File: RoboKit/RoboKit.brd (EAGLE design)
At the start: 160 x 100 mm, 27 parts, among them CON1 XT30UPB-M, CON2 XT30UPB-M, P1 B6B-PH-K, P2 B6B-PH-K, U1 SSM6J808R, X1 JST-XH-06-PIN-LONG-PAD, X2 JST-XH-06-PIN-LONG-PAD, X3 JST-XH-02-PIN-LONG-PAD, X4 JST-XH-02-PIN-LONG-PAD, X5 JST-XH-04-PIN-LONG-PAD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

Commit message: make_circuit
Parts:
- removed X1, X2: JST-XH-06-PIN-LONG-PAD, JST XH Connectors:JST-XH-06-PACKAGE-LONG-PAD
- added CONNECTOR1: RESISTER, resistor:RESISTER_SOCKET
- added S1: (no value), switch-omron:B3F-10XX
- added TC4052DP: (no value), ic-package:DIL16
- added X7: JST-XH-10-PIN-LONG-PAD, Rembrandt Electronics - JST XH Connectors v1-0:JST-XH-10-PACKAGE-LONG-PAD
- added X8: JST-XH-02-PIN-LONG-PAD, Rembrandt Electronics - JST XH Connectors v1-0:JST-XH-02-PACKAGE-LONG-PAD
- added X9: JST-XH-03-PIN-LONG-PAD, Rembrandt Electronics - JST XH Connectors v1-0:JST-XH-03-PACKAGE-LONG-PAD
- moved X5 143.9 mm to (66.4, 69.2)
- moved X6 143.3 mm to (66.4, 60.3)
- moved X4 105.9 mm to (21.6, 66.4)
- moved X3 91.8 mm to (8.57, 66.7)
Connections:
- removed net +5V: X1.2, X2.2
- removed net ADC0: U$1.31
- removed net ADC1: U$1.32
- removed net IO16: U$1.21
- removed net IO17: U$1.22
- removed net LINE: X1.3, X2.3
- removed net MD_INA_L: U$2.INA1, U$2.INA2
- removed net MD_INA_R: U$3.INA1, U$3.INA2
- removed net MD_INB_L: U$2.INB1, U$2.INB2
- removed net MD_INB_R: U$3.INB1, U$3.INB2
- removed net MOTER_A_L: X3.1
- removed net MOTER_A_R: X4.1
- removed net MOTER_B_L: X3.2
- removed net MOTER_B_R: X4.2
- removed net MUX0: X1.4, X2.4
- removed net MUX1: X1.5, X2.5
- removed net MUX2: X1.6, X2.6
- new net 0X: TC4052DP.12, X7.3
- new net 0Y: TC4052DP.1, X7.7
- new net 1X: TC4052DP.14, X7.4
- new net 1Y: TC4052DP.5, X7.8
- new net 2X: TC4052DP.15, X7.5
- new net 2Y: TC4052DP.2, X7.9
- new net 3X: TC4052DP.11, X7.6
- new net 3Y: TC4052DP.4, X7.10
- new net A: TC4052DP.10, U$1.21
- new net B: TC4052DP.9, U$1.22
- new net N$4: CONNECTOR1.2, S1.3
- new net X-COM: TC4052DP.13, U$1.32
- new net Y-COM: TC4052DP.3, U$1.31
- net 3V3: now also CONNECTOR1.1
- net GND: now also S1.2, TC4052DP.6, TC4052DP.7, TC4052DP.8, X7.1, X8.2, X9.2; no longer X1.1, X2.1
- net IO0: now also U$2.INA1, U$2.INB1
- net IO1: now also U$2.INA2, U$2.INB2
- net IO2: now also U$3.INA1, U$3.INB1
- net IO21: now also S1.4
- net IO3: now also U$3.INA2, U$3.INB2
- net IO7: now also X8.1
- net MOTOR_A_L: now also X3.1
- net MOTOR_A_R: now also X4.1
- net MOTOR_B_L: now also X3.2
- net MOTOR_B_R: now also X4.2
- net VBUS: now also TC4052DP.16, X7.2, X9.1
- net VOUT: now also X9.3
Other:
- board size 160 x 100 mm -> 134 x 82 mm

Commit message: make_okunishi_1
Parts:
- moved X4 80.3 mm to (98.7, 44.1), turned to 90 degrees
- moved U$3 72.0 mm to (88.3, 62.9)
- moved X9 54.3 mm to (31.1, 28.6)
- moved X6 50.8 mm to (100.3, 22.5), turned to 270 degrees
- moved X8 41.0 mm to (86.4, 44.5)
- moved U$4 40.5 mm to (34.9, 17.8)
- moved X3 35.2 mm to (35.6, 44.1), turned to 270 degrees
- moved U$2 30.7 mm to (46.4, 62.9)
- moved P1 30.1 mm to (98.7, 63.2), turned to 90 degrees
- moved U$1 29.2 mm to (66.4, 45.1)
- moved TC4052DP 27.6 mm to (47.0, 39.1), turned to 90 degrees
- moved X7 21.0 mm to (91.8, 22.2), turned to 270 degrees
- moved P2 18.6 mm to (35.6, 63.2), turned to 270 degrees
- moved S1 17.6 mm to (95.2, 76.5)
- moved CONNECTOR1 10.8 mm to (81.0, 74.3)
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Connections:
- net 3V3_EN: now also X6.1
- net VCC: no longer X6.1
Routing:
- net GND: track 0.00 -> 329.6 mm, vias 0 -> 3
- net SDA: track 0.00 -> 168.8 mm
- net VBUS: track 0.00 -> 159.1 mm, vias 0 -> 2
- net SCL: track 0.00 -> 155.0 mm
- net VCC: track 0.00 -> 139.1 mm
- net VOUT: track 30.6 -> 142.7 mm
- net 3Y: track 0.00 -> 89.4 mm
- net 3X: track 0.00 -> 83.4 mm
- net IO0: track 0.00 -> 76.8 mm
- net 0X: track 0.00 -> 74.8 mm, vias 0 -> 1
- net 2X: track 0.00 -> 74.6 mm
- net 1Y: track 0.00 -> 57.3 mm
- net IO21: track 0.00 -> 56.1 mm
- net 1X: track 0.00 -> 55.9 mm
- net 2Y: track 0.00 -> 54.3 mm
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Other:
- outline, holes or cut-outs redrawn

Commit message: 回路図の完成
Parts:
- added S2: (no value), switch:320-916
- moved CON2 77.6 mm to (38.1, 76.8)
- moved X6 63.7 mm to (66.0, 76.2), turned to 0 degrees
- moved X5 62.3 mm to (99.4, 22.9), turned to 270 degrees
- moved TC4052DP 42.0 mm to (87.3, 27.3)
- moved X7 28.3 mm to (67.0, 8.57), turned to 0 degrees
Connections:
- removed net IO10: U$1.14
- removed net IO11: U$1.15
- removed net IO12: U$1.16
- removed net IO13: U$1.17
- removed net IO4: U$1.6
- removed net IO5: U$1.7
- new net 5.0V: S2.2, X9.1
- net HALL_A_L: now also U$1.16
- net HALL_A_R: now also U$1.14
- net HALL_B_L: now also U$1.17
- net HALL_B_R: now also U$1.15
- net SCL: now also U$1.7
- net SDA: now also U$1.6
- net VBUS: now also S2.3; no longer X9.1
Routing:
- net GND: track 329.6 -> 2.79 mm, vias 3 -> 0
- net SDA: track 168.8 -> 1.30 mm
- net VBUS: track 159.1 -> 0.00 mm, vias 2 -> 0
- net SCL: track 155.0 -> 0.00 mm
- net VCC: track 139.1 -> 0.00 mm
- net VOUT: track 142.7 -> 30.7 mm
- net 3Y: track 89.4 -> 0.00 mm
- net 3X: track 83.4 -> 0.10 mm
- net IO0: track 76.8 -> 0.00 mm
- net 0X: track 74.8 -> 0.00 mm, vias 1 -> 0
- net 2X: track 74.6 -> 0.00 mm
- net 1Y: track 57.3 -> 0.00 mm
- net 1X: track 55.9 -> 0.00 mm
- net IO21: track 56.1 -> 0.89 mm
- net 2Y: track 54.3 -> 0.00 mm
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
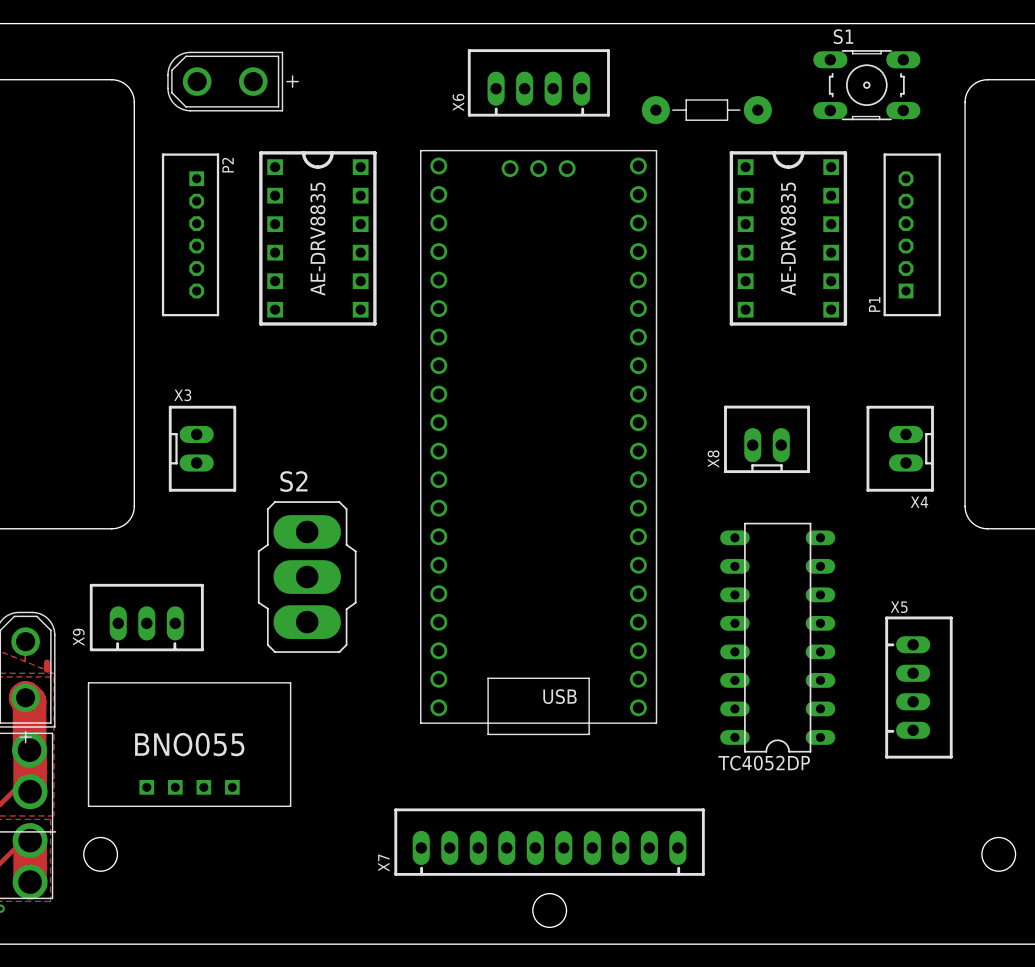
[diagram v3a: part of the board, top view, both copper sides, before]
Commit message: ボードのグランド以外を配置
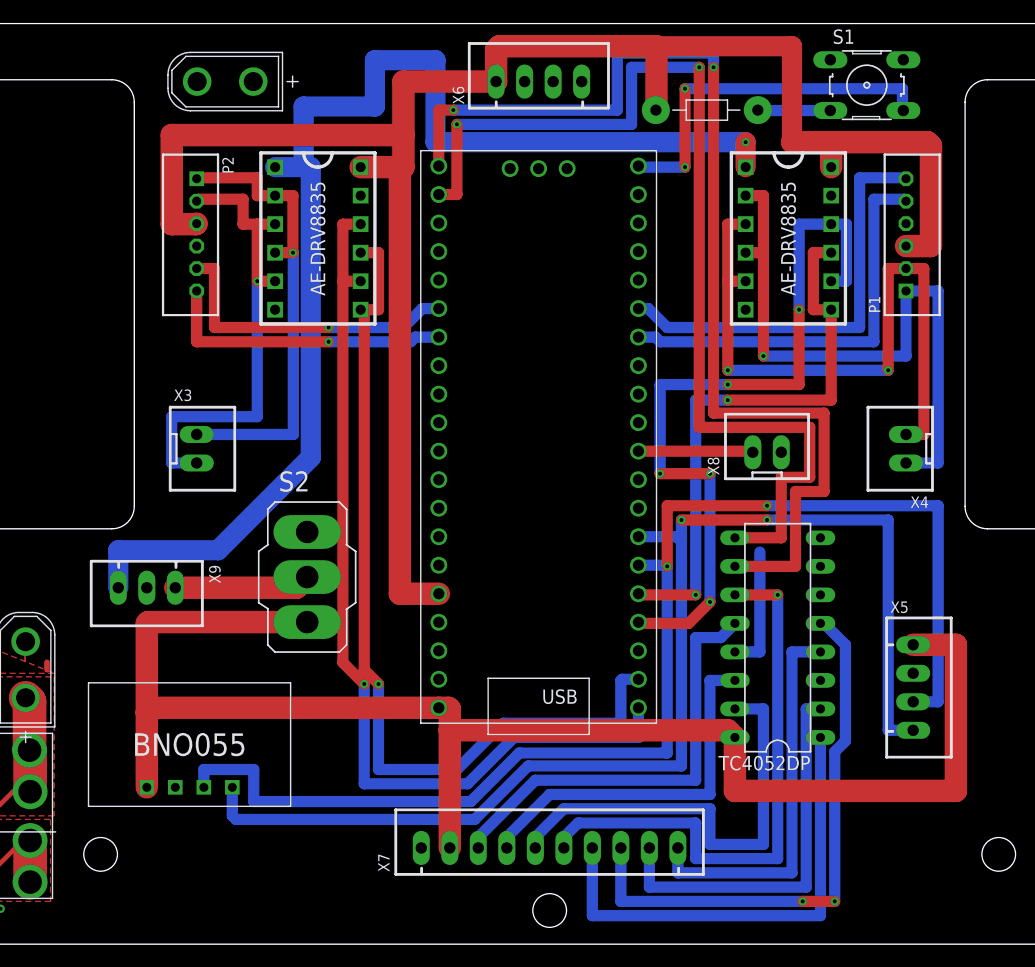
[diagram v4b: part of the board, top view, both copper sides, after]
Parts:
- moved X9 3.18 mm to (31.1, 31.8), turned to 180 degrees
- moved X8 0.64 mm to (86.4, 43.8)
- moved X6 0.63 mm to (66.0, 76.8)
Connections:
- removed net IO20: U$1.26
- removed net VCC: P1.3, P2.3, U$2.VCC, U$3.VCC, U$4.VIN
- new net IO12: U$1.16
- new net IO13: U$1.17
- net 3V3: now also P1.3, P2.3, U$2.VCC, U$3.VCC, X6.1
- net 3V3_EN: no longer X6.1
- net HALL_A_L: now also U$1.26; no longer U$1.16
- net HALL_B_L: now also U$1.27; no longer U$1.17
- net IO0: now also U$2.INA2; no longer U$2.INB1
- net IO1: now also U$2.INB1; no longer U$2.INA2
- net IO15: now also S1.4
- net IO2: now also U$3.INA2; no longer U$3.INB1
- net IO21: no longer S1.4, U$1.27
- net IO3: now also U$3.INB1; no longer U$3.INA2
- net MOTOR_A_L: now also U$2.AOUT2; no longer U$2.BOUT1
- net MOTOR_A_R: now also U$3.AOUT2; no longer U$3.BOUT1
- net MOTOR_B_L: now also U$2.BOUT1; no longer U$2.AOUT2
- net MOTOR_B_R: now also U$3.BOUT1; no longer U$3.AOUT2
- net VBUS: now also U$4.VIN
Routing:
- net 3V3: track 0.03 -> 161.4 mm
- net VBUS: track 0.00 -> 135.5 mm
- net SDA: track 1.30 -> 116.0 mm, vias 0 -> 2
- net VOUT: track 30.7 -> 142.1 mm, vias 0 -> 1
- net SCL: track 0.00 -> 109.9 mm, vias 0 -> 2
- net A: track 0.00 -> 98.0 mm, vias 0 -> 2
- net B: track 0.00 -> 93.0 mm, vias 0 -> 2
- net IO0: track 0.00 -> 82.6 mm, vias 0 -> 1
- net IO1: track 0.03 -> 78.6 mm, vias 0 -> 1
- net IO2: track 0.00 -> 68.3 mm, vias 0 -> 5
- net MOTOR_B_R: track 0.06 -> 59.1 mm, vias 0 -> 2
- net MOTOR_A_R: track 0.05 -> 57.0 mm, vias 0 -> 1
- net 3X: track 0.10 -> 51.0 mm, vias 0 -> 1
- net IO3: track 0.00 -> 50.9 mm, vias 0 -> 2
- net 1Y: track 0.00 -> 50.1 mm, vias 0 -> 2
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
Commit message: 線を斜めに配置
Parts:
- moved CON1 5.41 mm to (20.6, 29.8)
- moved U$7 5.08 mm to (20.3, 16.5)
- moved CON2 1.59 mm to (36.5, 76.8)
- moved X3 1.59 mm to (37.1, 44.1)
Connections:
- net VBUS: no longer S2.3, TC4052DP.16, U$4.VIN, X5.1, X7.2
- net VSYS: now also S2.3, TC4052DP.16, U$4.VIN, X5.1, X7.2
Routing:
- net X-COM: track 11.1 -> 153.6 mm, vias 0 -> 4
- net VSYS: track 0.00 -> 136.6 mm
- net VBUS: track 135.5 -> 0.00 mm
- net Y-COM: track 0.00 -> 117.3 mm, vias 0 -> 6
- net VIN: track 5.01 -> 97.6 mm, vias 0 -> 1
- net SDA: track 116.0 -> 161.1 mm, vias 2 -> 3
- net SCL: track 109.9 -> 152.6 mm, vias 2 -> 3
- net VOUT: track 142.1 -> 159.7 mm, vias 1 -> 2
- net 3V3: track 161.4 -> 154.4 mm
- net MOTOR_A_L: track 41.7 -> 36.0 mm
- net GND: track 2.52 -> 8.05 mm
- net V_HIGH: track 8.74 -> 13.4 mm
- net MOTOR_B_L: track 42.0 -> 37.3 mm
- net B: track 93.0 -> 89.8 mm
- net 3Y: track 34.6 -> 31.5 mm
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
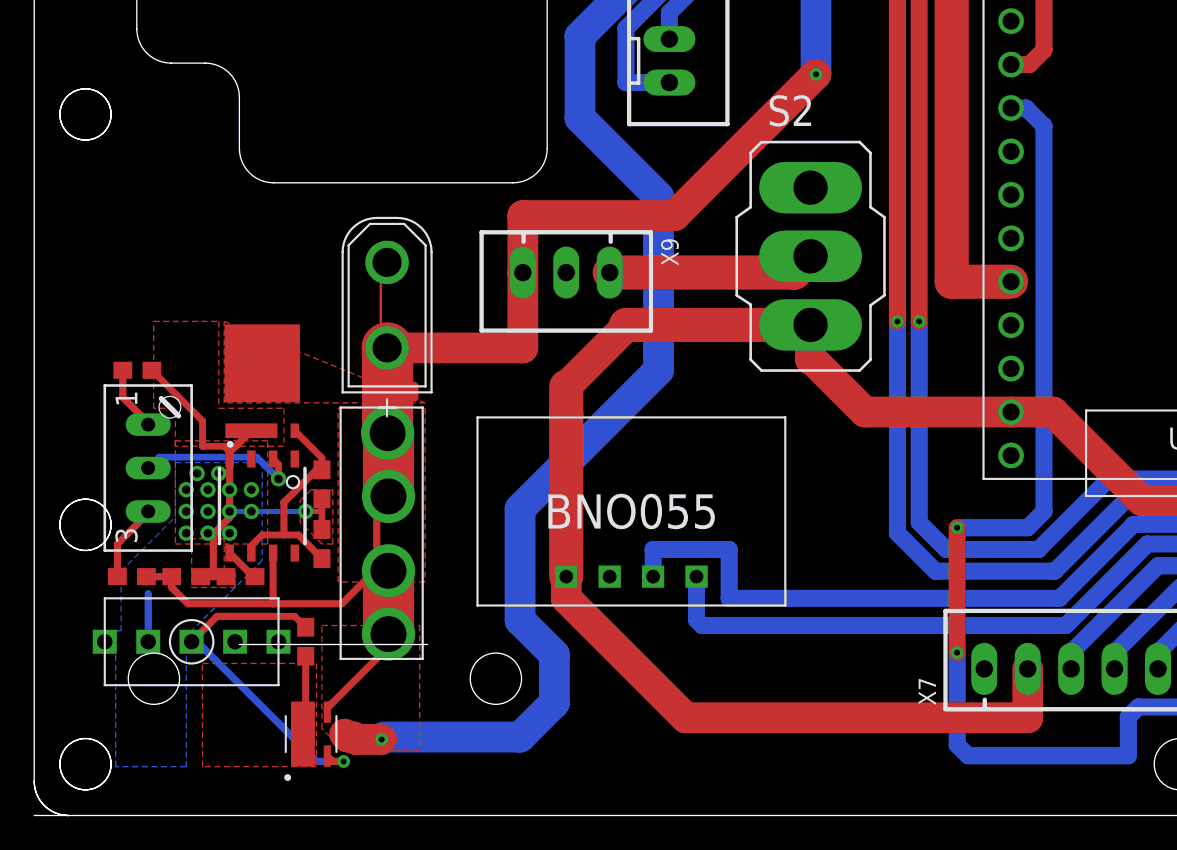
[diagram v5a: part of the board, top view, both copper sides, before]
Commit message: 保護回路の配線を設定
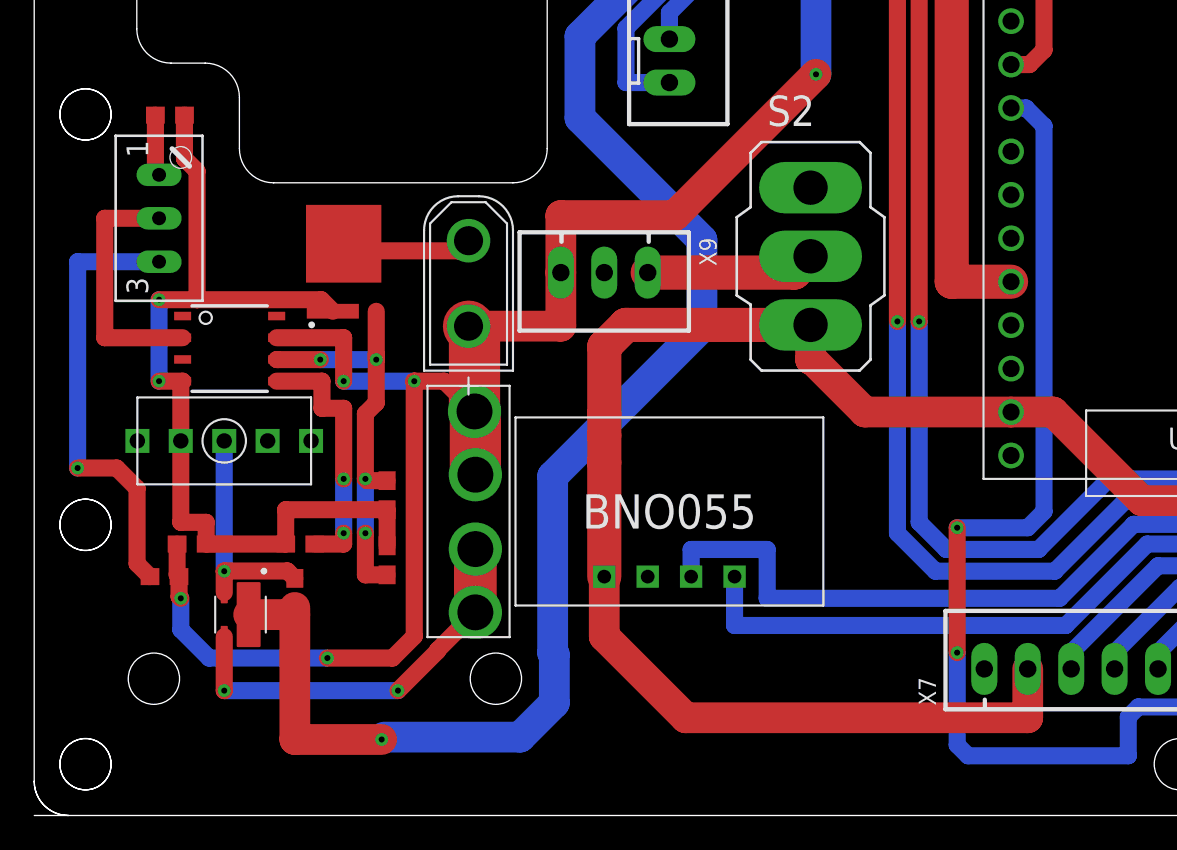
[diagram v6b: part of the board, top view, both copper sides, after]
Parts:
- moved R3 15.0 mm to (7.94, 41.0)
- moved R5 14.6 mm to (8.57, 34.9)
- moved U$9 11.9 mm to (11.1, 21.9)
- moved U$5 9.40 mm to (11.4, 27.3), turned to 0 degrees
- moved U$6 8.45 mm to (18.1, 32.4)
- moved U1 8.11 mm to (12.1, 11.7), turned to 270 degrees
- moved U$7 5.24 mm to (25.4, 17.8)
- moved CON1 4.93 mm to (25.4, 31.1)
- moved C11 3.98 mm to (15.6, 15.9)
- moved C7 3.93 mm to (20.6, 14.9)
- moved R2 3.86 mm to (20.6, 18.7)
- moved R4 2.93 mm to (15.2, 13.0)
- moved U$4 2.22 mm to (37.1, 17.8)
- moved X9 2.22 mm to (33.3, 31.8)
- moved C2 1.93 mm to (9.21, 15.9)
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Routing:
- net GND_IN: track 31.0 -> 53.4 mm, vias 14 -> 2
- net N$3: track 4.56 -> 26.3 mm, vias 0 -> 1
- net VOUT: track 159.7 -> 176.3 mm, vias 2 -> 6
- net N$5: track 2.06 -> 15.1 mm, vias 0 -> 2
- net N$6: track 13.2 -> 24.4 mm, vias 0 -> 4
- net V_HIGH: track 13.4 -> 23.5 mm, vias 0 -> 2
- net VIN: track 97.6 -> 106.1 mm
- net N$7: track 20.4 -> 13.2 mm
- net N$1: track 9.70 -> 14.7 mm, vias 1 -> 0
- net 5.0V: track 12.1 -> 9.92 mm
- net SDA: track 161.1 -> 158.9 mm
- net SCL: track 152.6 -> 150.6 mm
- net VSYS: track 136.6 -> 134.6 mm
- removed copper zone on layer 1, net GND
- removed copper zone on layer 1, net GND_IN
- removed copper zone on layer 16, net GND_IN
- removed copper zone on layer 1, net VIN
- removed copper zone on layer 1, net VOUT
- removed copper zone on layer 1, net V_HIGH
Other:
- outline, holes or cut-outs redrawn

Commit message: 一応完成
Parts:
- moved S1 2.71 mm to (92.7, 75.6)
- moved R3 0.95 mm to (6.99, 41.0)
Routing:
- net GND: track 8.26 -> 163.1 mm, vias 0 -> 6
- net 3V3: track 154.4 -> 168.9 mm
- net VSYS: track 134.6 -> 137.8 mm
- net X-COM: track 153.6 -> 156.4 mm
- net N$4: track 6.47 -> 4.33 mm
- net IO15: track 32.5 -> 30.6 mm, vias 2 -> 3
- net GND_IN: track 53.4 -> 54.8 mm
- net HALL_A_R: track 36.4 -> 36.3 mm, vias 0 -> 1
- net HALL_B_R: track 36.8 -> 36.7 mm, vias 0 -> 1
- added copper zone on layer 1, net GND
- added copper zone on layer 16, net GND
- added copper zone on layer 1, net GND_IN

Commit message: テスト2回目
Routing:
- net X-COM: track 156.4 -> 155.5 mm
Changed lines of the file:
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@@
 <wire x1="63.9835" y1="1.905" x2="55.245" y2="1.905" width="1" layer="16"/>
 <wire x1="53.975" y1="3.175" x2="55.245" y2="1.905" width="1" layer="16"/>
-<wire x1="70.1675" y1="2.469" x2="70.1675" y2="5.715" width="1" layer="16"/>
+<wire x1="70.1675" y1="2.469" x2="70.1675" y2="5.08" width="1" layer="16"/>
 <wire x1="70.1675" y1="2.469" x2="93.6625" y2="2.469" width="1" layer="16"/>
 <wire x1="93.6625" y1="16.51" x2="94.615" y2="17.4625" width="1" layer="16"/>
@@
 <wire x1="85.09" y1="37.12448125" x2="85.725" y2="36.48948125" width="1" layer="16"/>
 <wire x1="85.725" y1="36.48948125" x2="85.725" y2="26.035" width="1" layer="16"/>
-<wire x1="70.1675" y1="5.715" x2="69.5325" y2="6.35" width="1" layer="16"/>
-<wire x1="63.9835" y1="5.76345" x2="63.9835" y2="1.905" width="1" layer="16"/>
-<wire x1="69.5325" y1="6.35" x2="64.57005" y2="6.35" width="1" layer="16"/>
-<wire x1="64.57005" y1="6.35" x2="63.9835" y2="5.76345" width="1" layer="16"/>
+<wire x1="70.1675" y1="5.08" x2="68.8975" y2="6.35" width="1" layer="16"/>
+<wire x1="63.9835" y1="4.81095" x2="63.9835" y2="1.905" width="1" layer="16"/>
+<wire x1="68.8975" y1="6.35" x2="65.52255" y2="6.35" width="1" layer="16"/>
+<wire x1="65.52255" y1="6.35" x2="63.9835" y2="4.81095" width="1" layer="16"/>
 </signal>
 <signal name="0X">
